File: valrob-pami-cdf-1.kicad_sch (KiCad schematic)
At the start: 109 parts, among them J1 Conn_01x04, J10 Conn_01x04_Pin, J3 USB_C_Receptacle_USB2.0_14P, J4 Conn_01x02, M1 Motor_Servo, Q1 Q_NMOS, Q2 Q_NMOS, Q3 Q_NMOS, SW1 SW_SPST, SW3 SW_Push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

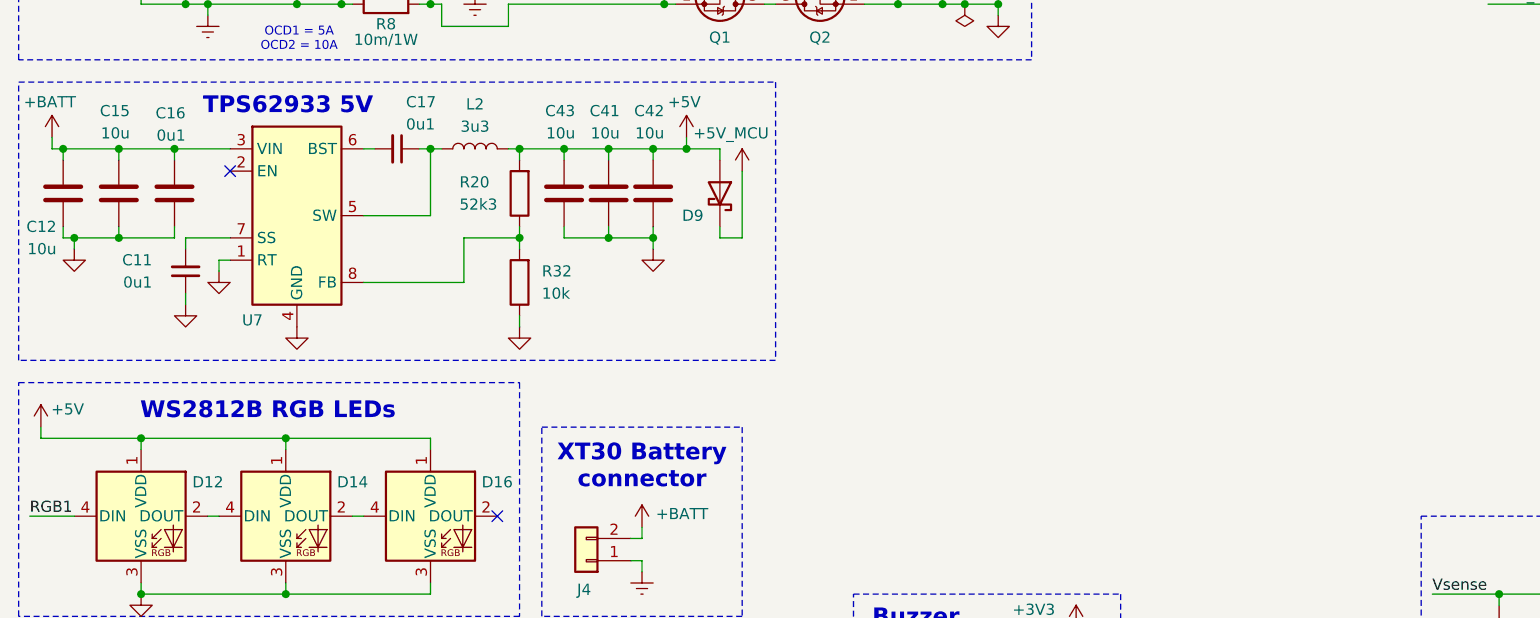
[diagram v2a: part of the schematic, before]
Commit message: schem: add VL53L0x tof sensor
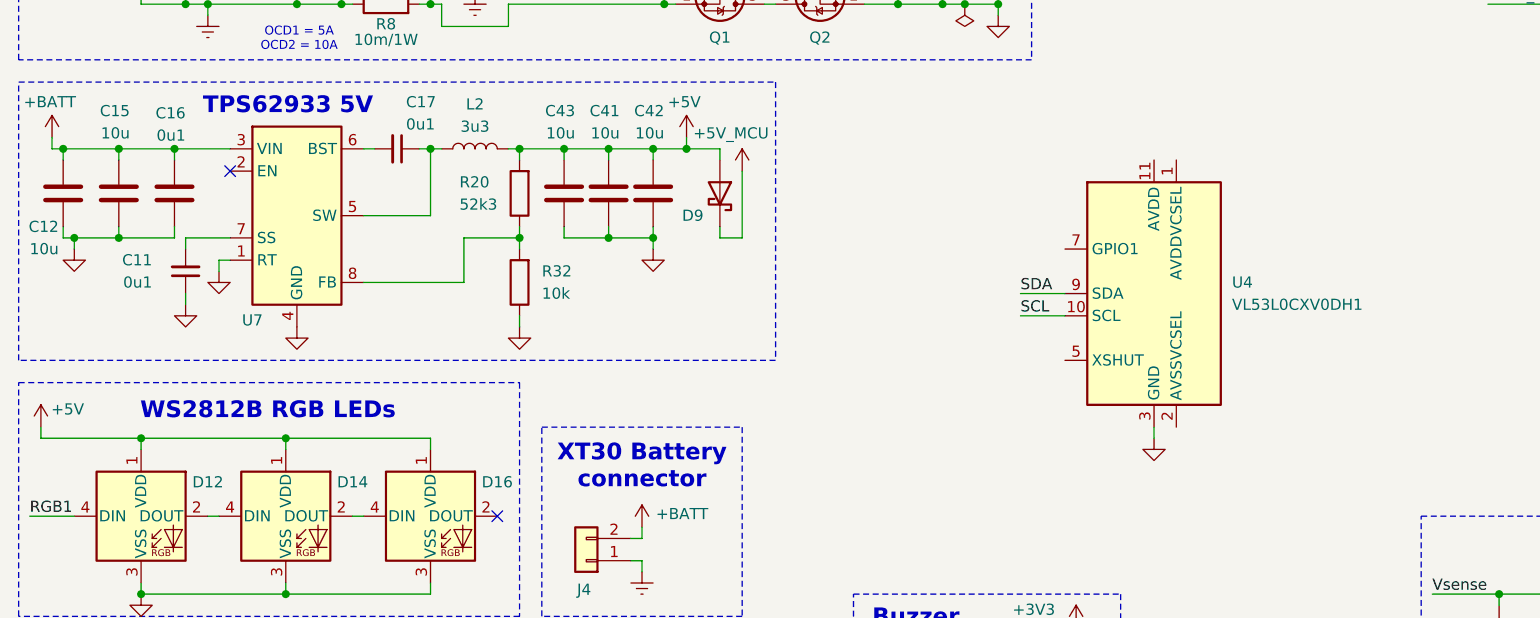
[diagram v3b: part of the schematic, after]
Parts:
- added U4: VL53L0CXV0DH1, Sensor_Distance:ST_VL53L1x, symbol Sensor_Distance:VL53L0CXV0DH1
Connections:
- net GND: now also U4.12 (GND), U4.3 (GND), U4.4 (GND), U4.6 (GND)
- new net SCL: U4.10 (SCL)
- new net SDA: U4.9 (SDA)
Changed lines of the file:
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@@
 	(wire
 		(pts
+			(xy 128.27 114.3) (xy 133.35 114.3)
+		)
+		(stroke
+			(width 0)
+			(type default)
+		)
+	)
+	(wire
+		(pts
 			(xy 45.72 77.47) (xy 45.72 78.74)
 		)
@@
 	(wire
 		(pts
+			(xy 128.27 111.76) (xy 133.35 111.76)
+		)
+		(stroke
+			(width 0)
+			(type default)
+		)
+	)
+	(wire
+		(pts
 			(xy 38.1 107.95) (xy 36.83 107.95)
 		)
@@
 	(wire
 		(pts
+			(xy 143.51 127) (xy 143.51 128.27)
+		)
+		(stroke
+			(width 0)
+			(type default)
+		)
+	)
+	(wire
+		(pts
 			(xy 176.53 44.45) (xy 185.42 44.45)
 		)
@@
 		)
 	)
+	(label "SCL"
+		(at 128.27 114.3 0)
+		(effects
+			(font
+				(size 1.27 1.27)
+			)
+			(justify left bottom)
+		)
+	)
 	(label "Vsense"
 		(at 175.26 146.05 0)
@@
 		)
 	)
+	(label "SDA"
+		(at 128.27 111.76 0)
+		(effects
+			(font
+				(size 1.27 1.27)
+			)
+			(justify left bottom)
+		)
+	)
 	(label "CHIP_PU"
 		(at 186.69 63.5 180)
@@
 		(dnp no)
 		(property "Reference" "C12"
-			(at 18.288 104.14 0)
+			(at 18.542 104.14 0)
 			(effects
 				(font
@@
 		)
 		(property "Value" "10u"
-			(at 18.288 106.68 0)
+			(at 18.542 106.68 0)
 			(effects
 				(font
@@
 	)
 	(symbol
+		(lib_id "Sensor_Distance:VL53L0CXV0DH1")
+		(at 143.51 111.76 0)
+		(unit 1)
+		(exclude_from_sim no)
+		(in_bom yes)
+		(on_board yes)
+		(dnp no)
+		(fields_autoplaced yes)
+		(property "Reference" "U4"
+			(at 152.4 110.4899 0)
+			(effects
+				(font
+					(size 1.27 1.27)
+				)
+				(justify left)
+			)
+		)
+		(property "Value" "VL53L0CXV0DH1"
+			(at 152.4 113.0299 0)
+			(effects
+				(font
+					(size 1.27 1.27)
+				)
+				(justify left)
+			)
+		)
+		(property "Footprint" "Sensor_Distance:ST_VL53L1x"
+			(at 160.655 125.73 0)
+			(effects
+				(font
+					(size 1.27 1.27)
+				)
+				(hide yes)
+			)
+		)
+		(property "Datasheet" "https://www.st.com/resource/en/datasheet/vl53l0x.pdf"
+			(at 146.05 111.76 0)
+			(effects
+				(font
+					(size 1.27 1.27)
+				)
+				(hide yes)
+			)
+		)
+		(property "Description" "2m distance ranging ToF sensor, Optical LGA12"
+			(at 143.51 111.76 0)
+			(effects
+				(font
+					(size 1.27 1.27)
+				)
+				(hide yes)
+			)
+		)
+		(property "Basic" "X"
+			(at 143.51 111.76 0)
+			(effects
+				(font
+					(size 1.27 1.27)
+				)
+				(hide yes)
+			)
+		)
+		(property "JLCPCB Part #" "C91199"
+			(at 143.51 111.76 0)
+			(effects
+				(font
+					(size 1.27 1.27)
+				)
+				(hide yes)
+			)
+		)
+		(property "Manufacturer" "STMicroelectronics"
+			(at 143.51 111.76 0)
+			(effects
+				(font
+					(size 1.27 1.27)
+				)
+				(hide yes)
+			)
+		)
+		(property "Manufacturer Part Number" "VL53L0CXV0DH/1"
+			(at 143.51 111.76 0)
+			(effects
+				(font
+					(size 1.27 1.27)
+				)
+				(hide yes)
+			)
+		)
+		(pin "10"
+		)
+		(pin "11"
+		)
+		(pin "3"
+		)
+		(pin "9"
+		)
+		(pin "1"
+		)
+		(pin "12"
+		)
+		(pin "2"
+		)
+		(pin "7"
+		)
+		(pin "5"
+		)
+		(pin "8"
+		)
+		(pin "4"
+		)
+		(pin "6"
+		)
+		(instances
+			(project ""
+				(path "/453def7e-2a78-4c3c-a4b7-f12883e5bdd2"
+					(reference "U4")
+					(unit 1)
+				)
+			)
+		)
+	)
+	(symbol
 		(lib_id "power:GND")
 		(at 165.1 193.04 0)
@@
 					(unit 1)
 				)
+			)
+		)
+	)
+	(symbol
+		(lib_id "power:GND")
+		(at 143.51 128.27 0)
+		(unit 1)
+		(exclude_from_sim no)
+		(in_bom yes)
+		(on_board yes)
+		(dnp no)
+		(property "Reference" "#PWR084"
+			(at 143.51 134.62 0)
+			(effects
+				(font
+					(size 1.27 1.27)
+				)
+				(hide yes)
+			)
+		)
+		(property "Value" "GND"
+			(at 143.51 132.588 0)
+			(effects
+				(font
+					(size 1.27 1.27)
+				)
+				(hide yes)
+			)
+		)
+		(property "Footprint" ""
+			(at 143.51 128.27 0)
+			(effects
+				(font
+					(size 1.27 1.27)
+				)
+				(hide yes)
+			)
+		)
+		(property "Datasheet" ""
+			(at 143.51 128.27 0)
+			(effects
+				(font
+					(size 1.27 1.27)
+				)
+				(hide yes)
+			)
+		)
+		(property "Description" "Power symbol creates a global label with name \"GND\" , ground"
+			(at 143.51 128.27 0)
+			(effects
+				(font
+					(size 1.27 1.27)
+				)
+				(hide yes)
+			)
+		)
+		(pin "1"
+		)
+		(instances
+			(project "valrob-pami-cdf-1"
+				(path "/453def7e-2a78-4c3c-a4b7-f12883e5bdd2"
+					(reference "#PWR084")
+					(unit 1)
+				)

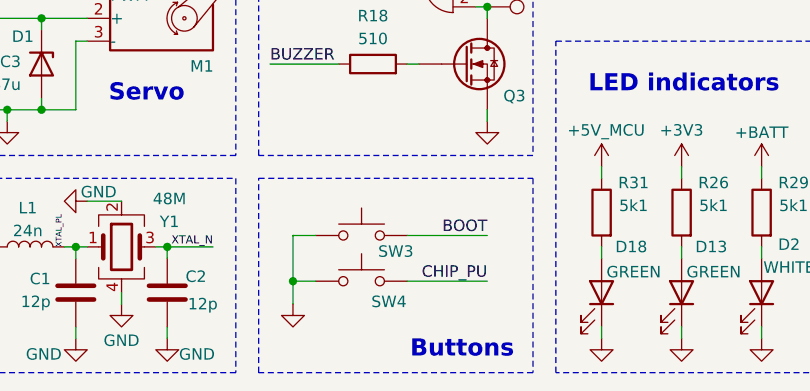
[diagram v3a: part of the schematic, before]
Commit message: schem: add EMS button
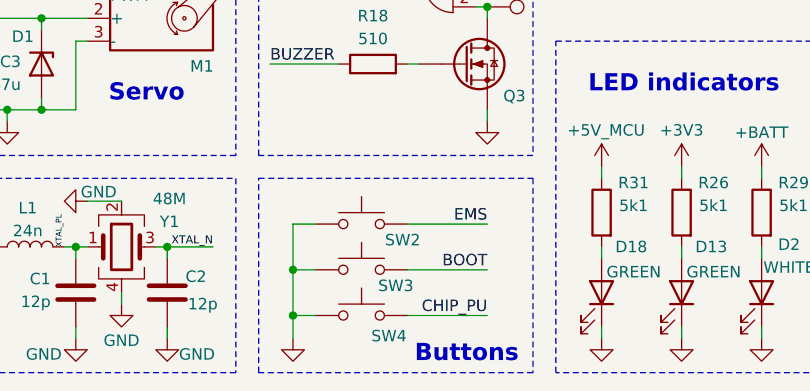
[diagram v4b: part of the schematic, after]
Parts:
- added SW2: SW_Push, Connector_JST:JST_XH_B2B-XH-A_1x02_P2.50mm_Vertical, symbol Switch:SW_Push
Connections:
- net EMS: now also SW2.2
- net GND: now also SW2.1
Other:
- moved on the sheet: SW3, SW4
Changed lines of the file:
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@@
 	(text "Buttons"
 		(exclude_from_sim no)
-		(at 131.826 194.31 0)
+		(at 132.334 194.818 0)
 		(effects
 			(font
@@
 	)
 	(junction
-		(at 113.03 186.69)
-		(diameter 0)
-		(color 0 0 0 0)
-	)
-	(junction
 		(at 62.23 36.83)
 		(diameter 0)
@@
 	)
 	(junction
+		(at 113.03 185.42)
+		(diameter 0)
+		(color 0 0 0 0)
+	)
+	(junction
 		(at 200.66 146.05)
 		(diameter 0)
@@
 	)
 	(junction
+		(at 113.03 190.5)
+		(diameter 0)
+		(color 0 0 0 0)
+	)
+	(junction
 		(at 195.58 146.05)
 		(diameter 0)
@@
 	(wire
 		(pts
-			(xy 113.03 181.61) (xy 115.57 181.61)
+			(xy 113.03 185.42) (xy 115.57 185.42)
 		)
 		(stroke
@@
 	(wire
 		(pts
+			(xy 125.73 180.34) (xy 134.62 180.34)
+		)
+		(stroke
+			(width 0)
+			(type default)
+		)
+	)
+	(wire
+		(pts
 			(xy 82.55 27.94) (xy 82.55 29.21)
 		)
@@
 	(wire
 		(pts
-			(xy 113.03 181.61) (xy 113.03 186.69)
-		)
-		(stroke
-			(width 0)
-			(type default)
-		)
-	)
-	(wire
-		(pts
 			(xy 181.61 78.74) (xy 189.23 78.74)
 		)
@@
 	(wire
 		(pts
-			(xy 125.73 186.69) (xy 134.62 186.69)
+			(xy 125.73 190.5) (xy 134.62 190.5)
 		)
 		(stroke
@@
 	(wire
 		(pts
+			(xy 113.03 180.34) (xy 113.03 185.42)
+		)
+		(stroke
+			(width 0)
+			(type default)
+		)
+	)
+	(wire
+		(pts
 			(xy 100.33 36.83) (xy 99.06 36.83)
 		)
@@
 	(wire
 		(pts
-			(xy 125.73 181.61) (xy 134.62 181.61)
+			(xy 125.73 185.42) (xy 134.62 185.42)
 		)
 		(stroke
@@
 	(wire
 		(pts
+			(xy 113.03 190.5) (xy 113.03 193.04)
+		)
+		(stroke
+			(width 0)
+			(type default)
+		)
+	)
+	(wire
+		(pts
 			(xy 99.06 36.83) (xy 99.06 34.29)
 		)
@@
 	(wire
 		(pts
+			(xy 115.57 180.34) (xy 113.03 180.34)
+		)
+		(stroke
+			(width 0)
+			(type default)
+		)
+	)
+	(wire
+		(pts
 			(xy 147.32 184.15) (xy 147.32 182.88)
 		)
@@
 	(wire
 		(pts
-			(xy 113.03 186.69) (xy 113.03 189.23)
+			(xy 113.03 185.42) (xy 113.03 190.5)
 		)
 		(stroke
@@
 	(wire
 		(pts
-			(xy 113.03 186.69) (xy 115.57 186.69)
+			(xy 113.03 190.5) (xy 115.57 190.5)
 		)
 		(stroke
@@
 	)
 	(label "BOOT"
-		(at 134.62 181.61 180)
+		(at 134.62 185.42 180)
 		(effects
 			(font
@@
 	)
 	(label "CHIP_PU"
-		(at 134.62 186.69 180)
+		(at 134.62 190.5 180)
 		(effects
 			(font
@@
 		)
 	)
+	(label "EMS"
+		(at 134.62 180.34 180)
+		(effects
+			(font
+				(size 1.27 1.27)
+			)
+			(justify right bottom)
+		)
+	)
 	(label "VDD_SPI"
 		(at 194.31 36.83 0)
@@
 	)
 	(symbol
+		(lib_id "Switch:SW_Push")
+		(at 120.65 180.34 0)
+		(unit 1)
+		(exclude_from_sim no)
+		(in_bom yes)
+		(on_board yes)
+		(dnp no)
+		(property "Reference" "SW2"
+			(at 125.222 182.118 0)
+			(effects
+				(font
+					(size 1.27 1.27)
+				)
+			)
+		)
+		(property "Value" "SW_Push"
+			(at 120.65 175.26 0)
+			(effects
+				(font
+					(size 1.27 1.27)
+				)
+				(hide yes)
+			)
+		)
+		(property "Footprint" "Connector_JST:JST_XH_B2B-XH-A_1x02_P2.50mm_Vertical"
+			(at 120.65 175.26 0)
+			(effects
+				(font
+					(size 1.27 1.27)
+				)
+				(hide yes)
+			)
+		)
+		(property "Datasheet" "~"
+			(at 120.65 175.26 0)
+			(effects
+				(font
+					(size 1.27 1.27)
+				)
+				(hide yes)
+			)
+		)
+		(property "Description" "Push button switch, generic, two pins"
+			(at 120.65 180.34 0)
+			(effects
+				(font
+					(size 1.27 1.27)
+				)
+				(hide yes)
+			)
+		)
+		(property "Manufacturer" "JST"
+			(at 120.65 180.34 0)
+			(effects
+				(font
+					(size 1.27 1.27)
+				)
+				(hide yes)
+			)
+		)
+		(property "Manufacturer Part Number" "B2B-XH-A(LF)(SN)"
+			(at 120.65 180.34 0)
+			(effects
+				(font
+					(size 1.27 1.27)
+				)
+				(hide yes)
+			)
+		)
+		(property "Basic" "Z"
+			(at 120.65 180.34 0)
+			(effects
+				(font
+					(size 1.27 1.27)
+				)
+				(hide yes)
+			)
+		)
+		(property "JLCPCB Part #" "C158012"
+			(at 120.65 180.34 0)
+			(effects
+				(font
+					(size 1.27 1.27)
+				)
+				(hide yes)
+			)
+		)
+		(pin "2"
+		)
+		(pin "1"
+		)
+		(instances
+			(project "valrob-pami-cdf-1"
+				(path "/453def7e-2a78-4c3c-a4b7-f12883e5bdd2"
+					(reference "SW2")
+					(unit 1)
+				)
+			)
+		)
+	)
+	(symbol
 		(lib_id "Device:C")
 		(at 68.58 27.94 270)
@@
 	(symbol
 		(lib_id "Switch:SW_Push")
-		(at 120.65 186.69 0)
+		(at 120.65 190.5 0)
 		(unit 1)
 		(exclude_from_sim no)
@@
 		(dnp no)
 		(property "Reference" "SW4"
-			(at 123.698 188.976 0)
+			(at 123.698 192.786 0)
 			(effects
 				(font
@@
 		)
 		(property "Value" "SW_Push"
-			(at 120.65 181.61 0)
+			(at 120.65 185.42 0)
 			(effects
 				(font
@@
 		)
 		(property "Footprint" "Button_Switch_SMD:SW_SPST_TS-1088-xR020"
-			(at 120.65 181.61 0)
+			(at 120.65 185.42 0)
 			(effects
 				(font
@@
 		)
 		(property "Datasheet" "~"
-			(at 120.65 181.61 0)
+			(at 120.65 185.42 0)
 			(effects
 				(font
@@
 		)
 		(property "Description" "Push button switch, generic, two pins"
-			(at 120.65 186.69 0)
+			(at 120.65 190.5 0)
 			(effects
 				(font
@@
 		)
 		(property "Manufacturer" "XUNPU"
-			(at 120.65 186.69 0)
+			(at 120.65 190.5 0)
 			(effects
 				(font
@@
 		)
 		(property "Manufacturer Part Number" "TS-1088-AR02016"
-			(at 120.65 186.69 0)
+			(at 120.65 190.5 0)
 			(effects
 				(font
@@
 		)
 		(property "Basic" "Y"
-			(at 120.65 186.69 0)
+			(at 120.65 190.5 0)
 			(effects
 				(font
@@
 		)
 		(property "JLCPCB Part #" "C720477"
-			(at 120.65 186.69 0)
+			(at 120.65 190.5 0)
 			(effects
 				(font
@@
 	(symbol
 		(lib_id "power:GND")
-		(at 113.03 189.23 0)
+		(at 113.03 193.04 0)
 		(unit 1)
 		(exclude_from_sim no)
@@
 		(fields_autoplaced yes)
 		(property "Reference" "#PWR040"
-			(at 113.03 195.58 0)
+			(at 113.03 199.39 0)
 			(effects
 				(font
@@
 		)
 		(property "Value" "GND"
-			(at 113.03 194.31 0)
+			(at 113.03 198.12 0)
 			(effects
 				(font
@@
 		)
 		(property "Footprint" ""
-			(at 113.03 189.23 0)
+			(at 113.03 193.04 0)
 			(effects
 				(font
@@
 		)
 		(property "Datasheet" ""
-			(at 113.03 189.23 0)
+			(at 113.03 193.04 0)
 			(effects
 				(font
@@
 		)
 		(property "Description" "Power symbol creates a global label with name \"GND\" , ground"
-			(at 113.03 189.23 0)
+			(at 113.03 193.04 0)
 			(effects
 				(font
@@
 	(symbol
 		(lib_id "Switch:SW_Push")
-		(at 120.65 181.61 0)
+		(at 120.65 185.42 0)
 		(unit 1)
 		(exclude_from_sim no)
@@
 		(dnp no)
 		(property "Reference" "SW3"
-			(at 124.46 183.388 0)
+			(at 124.46 187.198 0)
 			(effects
 				(font
@@
 		)
 		(property "Value" "SW_Push"
-			(at 120.65 176.53 0)
+			(at 120.65 180.34 0)
 			(effects
 				(font
@@
 		)
 		(property "Footprint" "Button_Switch_SMD:SW_SPST_TS-1088-xR020"
-			(at 120.65 176.53 0)
+			(at 120.65 180.34 0)
 			(effects
 				(font
@@
 		)
 		(property "Datasheet" "~"
-			(at 120.65 176.53 0)
+			(at 120.65 180.34 0)
 			(effects
 				(font
@@
 		)
 		(property "Description" "Push button switch, generic, two pins"
-			(at 120.65 181.61 0)
+			(at 120.65 185.42 0)
 			(effects
 				(font
@@
 		)
 		(property "Manufacturer" "XUNPU"
-			(at 120.65 181.61 0)
+			(at 120.65 185.42 0)
 			(effects
 				(font
@@
 		)
 		(property "Manufacturer Part Number" "TS-1088-AR02016"
-			(at 120.65 181.61 0)
+			(at 120.65 185.42 0)
 			(effects
 				(font
@@
 		)
 		(property "Basic" "Y"
-			(at 120.65 181.61 0)
+			(at 120.65 185.42 0)
 			(effects
 				(font
@@
 		)
 		(property "JLCPCB Part #" "C720477"
-			(at 120.65 181.61 0)
+			(at 120.65 185.42 0)
 			(effects
 				(font

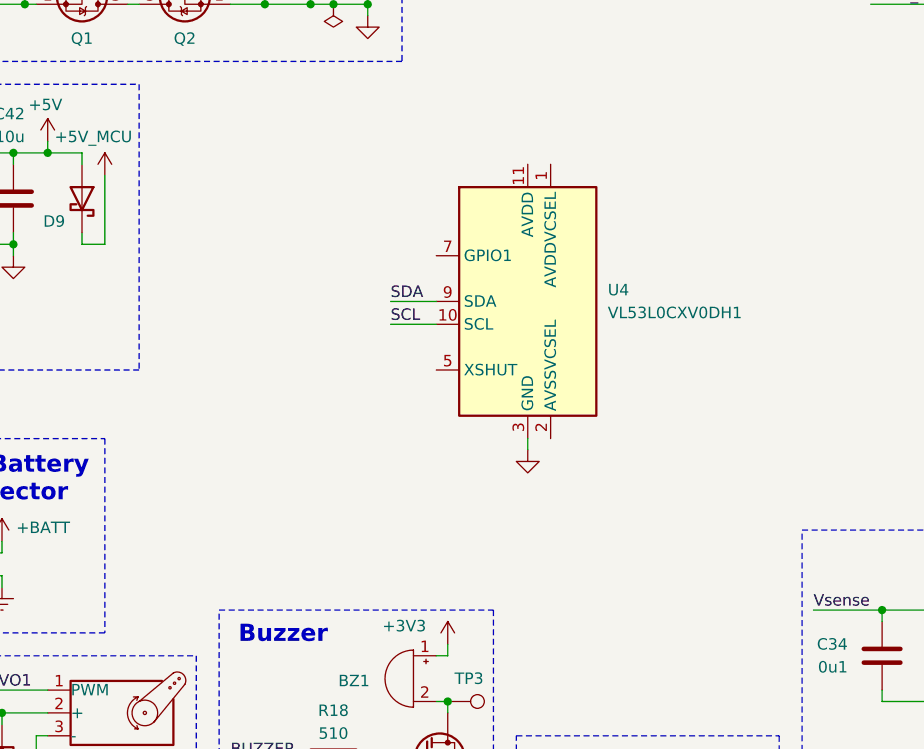
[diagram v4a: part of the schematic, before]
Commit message: schem: add VL53L0X ToF sensor
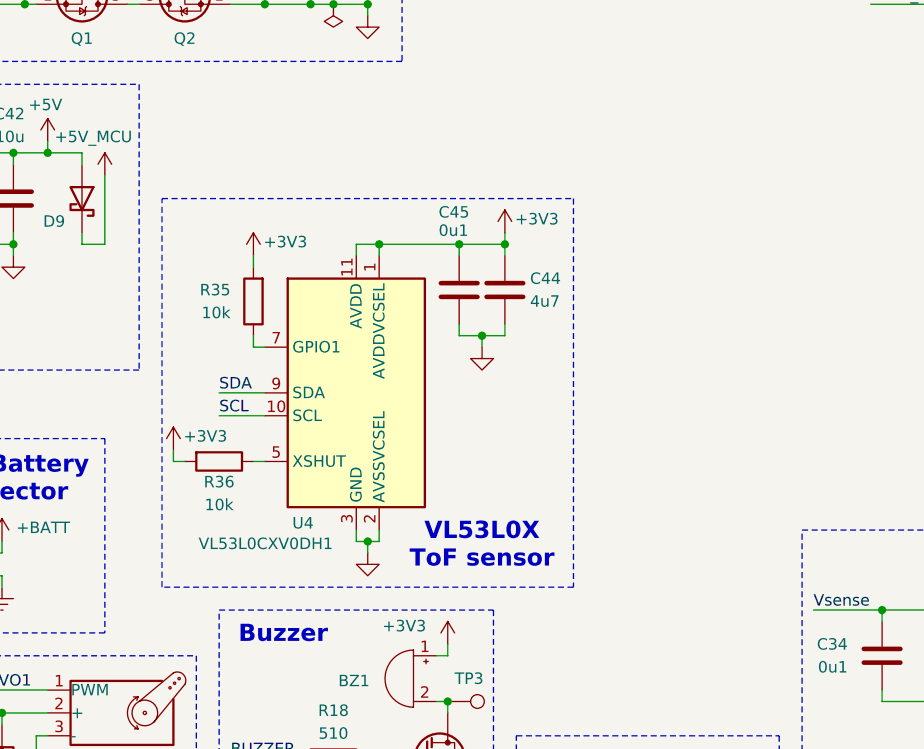
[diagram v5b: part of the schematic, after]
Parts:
- added C44: 4u7, Capacitor_SMD:C_0402_1005Metric, symbol Device:C
- added C45: 0u1, Capacitor_SMD:C_0402_1005Metric, symbol Device:C
- added R35, R36: 10k, Resistor_SMD:R_0402_1005Metric, symbol Device:R
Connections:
- net +3V3: now also U4.1 (AVDDVCSEL), U4.11 (AVDD), C44.1, C45.1, R35.2, R36.2
- net GND: now also U4.2 (AVSSVCSEL), C44.2, C45.2
- net at U4.5 (XSHUT): now also R36.1
- net at U4.7 (GPIO1): now also R35.1
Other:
- note added: "VL53L0X ToF sensor"
- moved on the sheet: U4
